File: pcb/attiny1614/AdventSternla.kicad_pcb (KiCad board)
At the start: 2 copper layers, 15 parts, among them J1 5V In, J2 GPIO_C, J3 UPDI, J4 GPIO_A, J5 GPIO_B, J6 NeoPixel Data, J7 Power Out, U1 ATTINY1614

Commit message: Initial layout completed
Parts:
- removed C1: 2200μF 25V, Capacitors_ThroughHole:CP_Radial_D13.0mm_P5.00mm
- removed C2: 1μF 16V, Capacitors_SMD:C_0805_HandSoldering
- removed C3: 100nF 50V, Capacitors_SMD:C_0805_HandSoldering
- removed D1: 5V6 Zener, Diodes_SMD:D_SOT-23_ANK
- removed J1: 5V In, Pin_Headers:Pin_Header_Straight_1x03_Pitch2.54mm
- removed J2: GPIO_C, Pin_Headers:Pin_Header_Straight_1x04_Pitch2.54mm
- removed J3: UPDI, Pin_Headers:Pin_Header_Straight_2x03_Pitch2.54mm
- removed J4: GPIO_A, Pin_Headers:Pin_Header_Straight_1x03_Pitch2.54mm
- removed J5: GPIO_B, Pin_Headers:Pin_Header_Straight_1x04_Pitch2.54mm
- removed J6: NeoPixel Data, Pin_Headers:Pin_Header_Straight_1x02_Pitch2.54mm
- removed J7: Power Out, Pin_Headers:Pin_Header_Straight_1x02_Pitch2.54mm
- removed R1: 250Ω 0.5W, Resistors_SMD:R_1210_HandSoldering
- removed R2: 47kΩ, Resistors_SMD:R_0805_HandSoldering
- removed R3: 4k7Ω, Resistors_SMD:R_0805_HandSoldering
- removed U1: ATTINY1614, SMD_Packages:SOIC-14_N
- added C101: 100nF 50V, Capacitors_SMD:C_0805_HandSoldering, F.Cu at (145.5, 94.5)
- added C102: 1000μF 25V, advent_sternla:CP_Radial_L21.0mm_D13.0mm_P5.00mm_Horizontal, B.Cu at (141.0, 95.5)
- added C103: 1μF 16V, Capacitors_SMD:C_0805_HandSoldering, F.Cu at (149.0, 100.0)
- added D101: 1N4148WSTR, Diodes_SMD:D_SOD-323, F.Cu at (144.5, 100.0)
- added G***: LOGO, advent_sternla:MyBasic_rounded_50_1, F.Cu at (136.8, 103.3)
- added J101: UPDI, advent_sternla:PRG_TC2030-IDC-NL, F.Cu at (163.5, 104.0)
- added J102: NeoPixel Data, Pin_Headers:Pin_Header_Straight_1x02_Pitch2.54mm, F.Cu at (167.9, 93.0)
- added J103: Power Out, Pin_Headers:Pin_Header_Straight_1x02_Pitch2.54mm, F.Cu at (167.9, 98.0)
- added J104: 5V In, advent_sternla:CONN_PWR_JACK_1_3X3_5MM_SOLDER, F.Cu at (143.6, 87.1)
- added J105: GPIO_A, Pin_Headers:Pin_Header_Straight_1x03_Pitch2.54mm, F.Cu at (156.2, 86.2)
- added J106: GPIO_B, Pin_Headers:Pin_Header_Straight_1x04_Pitch2.54mm, F.Cu at (148.0, 104.5)
- added J107: GPIO_C, Pin_Headers:Pin_Header_Straight_1x04_Pitch2.54mm, F.Cu at (167.4, 86.2)
- added R101: 4k7Ω, Resistors_SMD:R_0805_HandSoldering, F.Cu at (163.5, 91.0)
- added R102: 47kΩ, Resistors_SMD:R_0805_HandSoldering, F.Cu at (148.0, 94.5)
- added U101: ATTINY1614, SMD_Packages:SOIC-14_N, F.Cu at (156.0, 95.0)
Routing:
- net /5V: track 0.00 -> 56.1 mm
- net /VDD: track 0.00 -> 42.2 mm
- net /PDI_DATA: track 0.00 -> 27.5 mm, vias 0 -> 2
- net /PA1: track 0.00 -> 16.9 mm, vias 0 -> 1
- net /PB0: track 0.00 -> 15.9 mm
- net /PB2: track 0.00 -> 13.5 mm
- net /PB3: track 0.00 -> 13.3 mm
- net /PA4: track 0.00 -> 9.05 mm
- net /PB1: track 0.00 -> 8.85 mm
- net /PA5: track 0.00 -> 7.93 mm
- net /PA6: track 0.00 -> 7.41 mm
- net /PA3: track 0.00 -> 6.90 mm
- net /PA7: track 0.00 -> 6.88 mm
- net /PA2: track 0.00 -> 6.48 mm
- net /NP_DATA: track 0.00 -> 4.44 mm
- added copper zone on F.Cu, net GND
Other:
- board outline added: 35.6 x 22.4 mm
- net class Default: clearance 0.2 -> 0.1524; trace_width 0.25 -> 0.1524; via_dia 0.6 -> 0.6858; via_drill 0.4 -> 0.3302
- rule pad_to_mask_clearance: 0.2 -> 0
- rule trace_clearance: 0.2 -> 0.1524
- rule trace_min: 0.2 -> 0.1524
- rule via_min_drill: 0.3 -> 0.3302
- rule via_min_size: 0.4 -> 0.6858
- board text added: "+ 5V Out"
- board text added: "5V In"
- board text added: "Data GND Out"
- board text added: "NeoPixel Driver 2L_1"
- board text added: "UDPI"

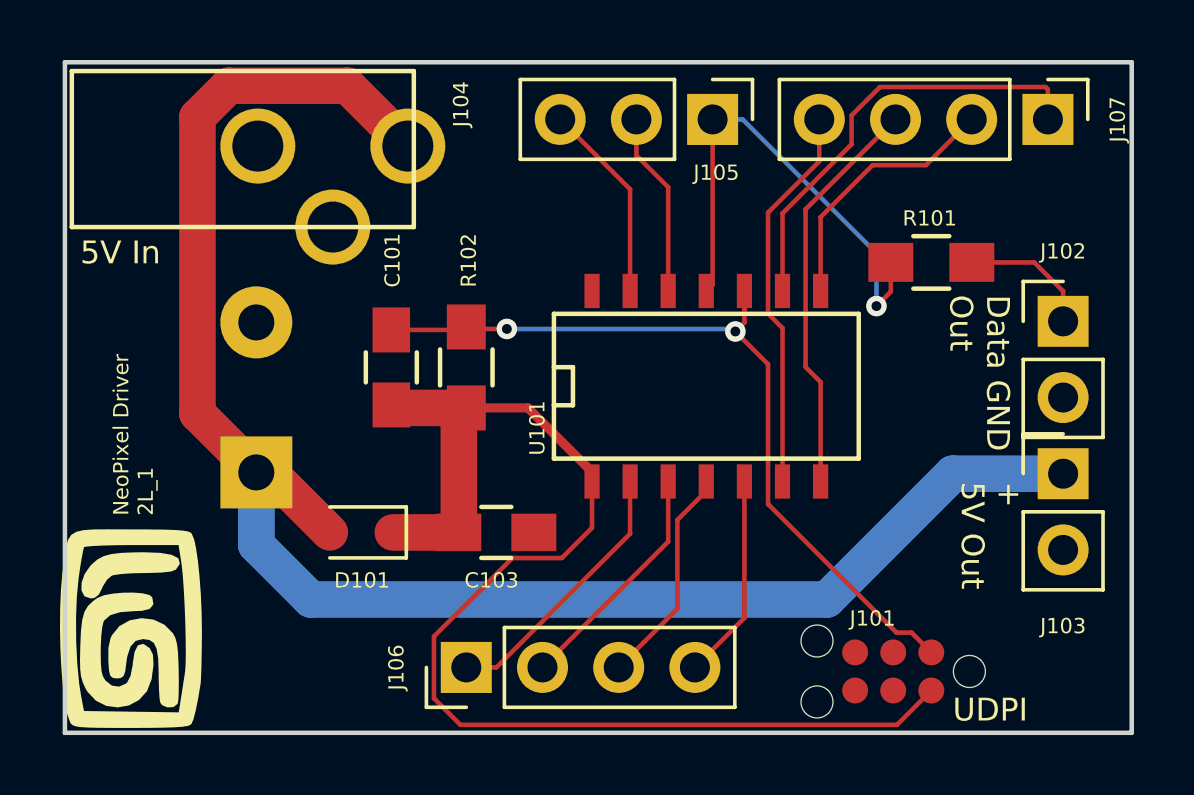
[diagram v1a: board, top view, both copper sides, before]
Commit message: Added some more nomenclature for the pin headers
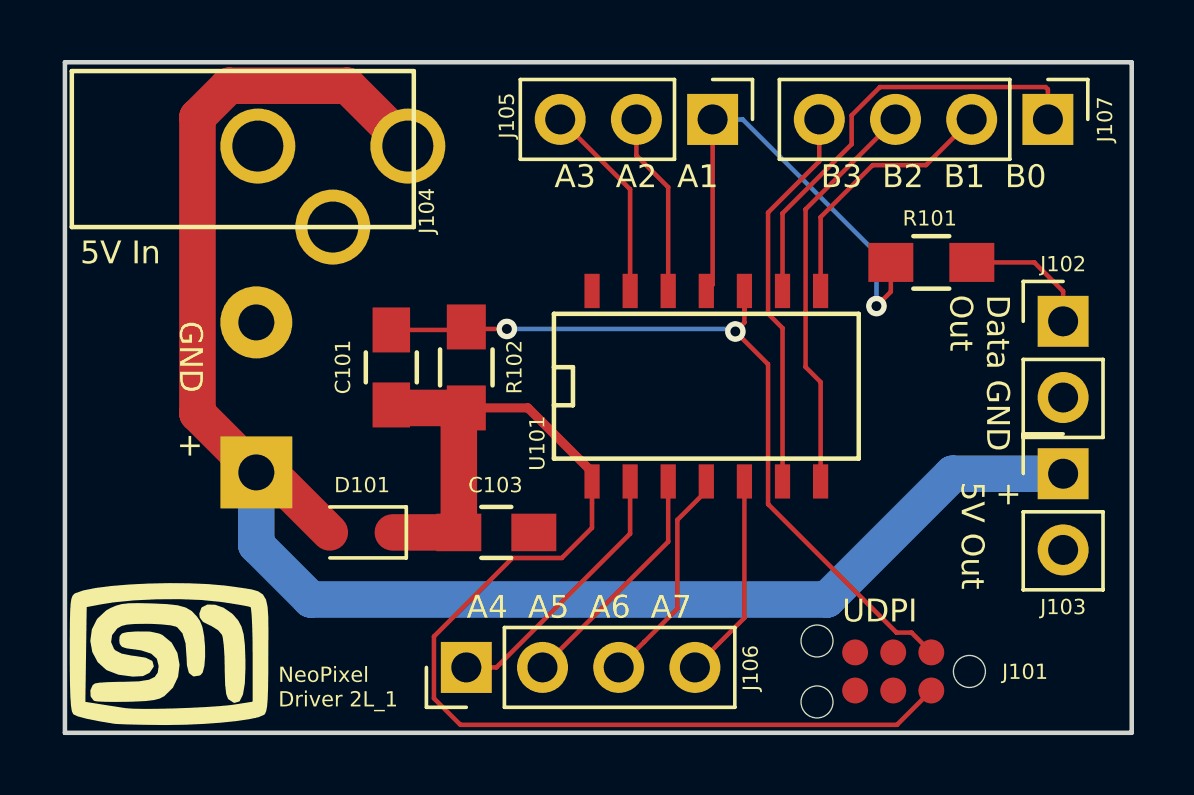
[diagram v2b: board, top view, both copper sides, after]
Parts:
- added G***: LOGO, advent_sternla:MyBasic_rounded_50_1, B.Cu at (138.4, 104.0)
- added G***: LOGO, advent_sternla:KiCad-Logo, B.Cu at (163.8, 104.3)
- moved G*** 1.48 mm to (138.0, 104.0), turned to 0 degrees
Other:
- board text added: "A3 A2 A1"
- board text added: "A4 A5 A6 A7"
- board text added: "B3 B2 B1 B0"
- board text added: "GND +"

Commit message: Added Gerbers and sent to OSH Park
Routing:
- net /5V: track 56.1 -> 49.5 mm
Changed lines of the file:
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@@
 (kicad_pcb (version 4) (host pcbnew 4.0.7)
   (general
-    (links 0)
+    (links 31)
     (no_connects 0)
-    (area 134.544999 84.252999 170.255001 106.755001)
+    (area 134.422599 73.0605 170.743639 107.1623)
     (thickness 1.6)
     (drawings 13)
-    (tracks 101)
+    (tracks 99)
     (zones 0)
     (modules 17)
@@
     (pad_to_mask_clearance 0)
     (aux_axis_origin 0 0)
-    (visible_elements FFFEFF7F)
+    (visible_elements FFFEEF7F)
     (pcbplotparams
-      (layerselection 0x00030_80000001)
+      (layerselection 0x010f0_80000001)
       (usegerberextensions false)
       (excludeedgelayer true)
@@
       (psa4output false)
       (plotreference true)
-      (plotvalue true)
+      (plotvalue false)
       (plotinvisibletext false)
       (padsonsilk false)
@@
       (outputformat 1)
       (mirror false)
-      (drillshape 1)
+      (drillshape 0)
       (scaleselection 1)
-      (outputdirectory ""))
+      (outputdirectory gerber/))
   )
   (net 0 "")
@@
       (rotate (xyz 0 0 0))
     )
-  )
-  (module advent_sternla:CP_Radial_L21.0mm_D13.0mm_P5.00mm_Horizontal (layer B.Cu)
-    (at 141 95.5)
-    (descr "CP, Radial series, Radial, Horizontal, pin pitch=5mm, , length*diameter=21*13mm^2, Electrolytic Capacitor")
-    (tags "CP Radal series Radial Horizontal pin pitch 5mm  length 21mm diameter 13mm Electrolytic Capacitor")
-    (fp_text reference C102 (at 14 0) (layer B.SilkS)
-      (effects (font (size 0.508 0.508) (thickness 0.127)) (justify mirror))
-    )
-    (fp_text value "1000μF 25V" (at 14 -5.06) (layer B.Fab)
-      (effects (font (size 0.508 0.508) (thickness 0.127)) (justify mirror))
-    )
-    (fp_line (start 0 -2.5) (end 3.5 -2.5) (layer B.Fab) (width 0.1))
-    (fp_line (start 1.38 -2.5) (end 3.44 -2.5) (layer B.SilkS) (width 0.12))
-    (fp_line (start 3.5 6.45) (end 3.5 -6.45) (layer B.Fab) (width 0.1))
-    (fp_line (start 24.5 6.45) (end 24.5 -6.45) (layer B.Fab) (width 0.1))
-    (fp_line (start 3.5 6.45) (end 5.24 6.45) (layer B.Fab) (width 0.1))
-    (fp_line (start 5.25 6.44) (end 6.15 5.54) (layer B.Fab) (width 0.1))
-    (fp_line (start 6.15 5.54) (end 7.05 6.44) (layer B.Fab) (width 0.1))
-    (fp_line (start 7.04 6.45) (end 24.5 6.45) (layer B.Fab) (width 0.1))
-    (fp_line (start 3.5 -6.45) (end 5.24 -6.45) (layer B.Fab) (width 0.1))
-    (fp_line (start 5.23 -6.44) (end 6.13 -5.54) (layer B.Fab) (width 0.1))
-    (fp_line (start 6.13 -5.54) (end 7.03 -6.44) (layer B.Fab) (width 0.1))
-    (fp_line (start 7.04 -6.45) (end 24.5 -6.45) (layer B.Fab) (width 0.1))
-    (fp_line (start 0 2.5) (end 3.5 2.5) (layer B.Fab) (width 0.1))
-    (fp_line (start 4.06 2.46) (end 5.86 2.46) (layer B.Fab) (width 0.1))
-    (fp_line (start 4.96 3.36) (end 4.96 1.56) (layer B.Fab) (width 0.1))
-    (fp_line (start 4.06 2.46) (end 5.86 2.46) (layer B.SilkS) (width 0.12))
-    (fp_line (start 4.96 3.36) (end 4.96 1.56) (layer B.SilkS) (width 0.12))
-    (fp_line (start 3.44 6.5) (end 3.44 -6.5) (layer B.SilkS) (width 0.12))
-    (fp_line (start 24.56 6.5) (end 24.56 -6.5) (layer B.SilkS) (width 0.12))
-    (fp_line (start 3.44 6.5) (end 5.24 6.5) (layer B.SilkS) (width 0.12))
-    (fp_line (start 5.25 6.5) (end 6.15 5.6) (layer B.SilkS) (width 0.12))
-    (fp_line (start 6.15 5.6) (end 7.05 6.5) (layer B.SilkS) (width 0.12))
-    (fp_line (start 7.04 6.5) (end 24.56 6.5) (layer B.SilkS) (width 0.12))
-    (fp_line (start 3.44 -6.5) (end 5.24 -6.5) (layer B.SilkS) (width 0.12))
-    (fp_line (start 5.23 -6.5) (end 6.13 -5.6) (layer B.SilkS) (width 0.12))
-    (fp_line (start 6.13 -5.6) (end 7.03 -6.5) (layer B.SilkS) (width 0.12))
-    (fp_line (start 7.04 -6.5) (end 24.56 -6.5) (layer B.SilkS) (width 0.12))
-    (fp_line (start 1.38 2.5) (end 3.44 2.5) (layer B.SilkS) (width 0.12))
-    (fp_line (start -1.45 7) (end -1.45 -7) (layer B.CrtYd) (width 0.05))
-    (fp_line (start -1.45 -7) (end 25 -7) (layer B.CrtYd) (width 0.05))
-    (fp_line (start 25 -7) (end 25 7) (layer B.CrtYd) (width 0.05))
-    (fp_line (start 25 7) (end -1.45 7) (layer B.CrtYd) (width 0.05))
-    (fp_text user %R (at 14 0) (layer B.Fab)
-      (effects (font (size 0.508 0.508) (thickness 0.127)) (justify mirror))
-    )
-    (pad 1 thru_hole rect (at 0 2.5) (size 2.4 2.4) (drill 1.2) (layers *.Cu *.Mask)
-      (net 1 /5V))
-    (pad 2 thru_hole oval (at 0 -2.5) (size 2.4 2.4) (drill 1.2) (layers *.Cu *.Mask)
-      (net 2 GND))
   )
   (module Capacitors_SMD:C_0805_HandSoldering (layer F.Cu)
@@
       (xy -2.775391 -0.969684)) (layer B.SilkS) (width 0.1))
   )
+  (module advent_sternla:CP_Radial_L21.0mm_D13.0mm_P5.00mm_Horizontal (layer B.Cu)
+    (at 141 95.5)
+    (descr "CP, Radial series, Radial, Horizontal, pin pitch=5mm, , length*diameter=21*13mm^2, Electrolytic Capacitor")
+    (tags "CP Radal series Radial Horizontal pin pitch 5mm  length 21mm diameter 13mm Electrolytic Capacitor")
+    (fp_text reference C102 (at 14 0) (layer B.SilkS)
+      (effects (font (size 1 1) (thickness 0.15)) (justify mirror))
+    )
+    (fp_text value "1000μF 25V" (at 14 -5.06) (layer B.Fab)
+      (effects (font (size 1 1) (thickness 0.15)) (justify mirror))
+    )
+    (fp_line (start 0 -2.5) (end 3.5 -2.5) (layer B.Fab) (width 0.1))
+    (fp_line (start 1.38 -2.5) (end 3.44 -2.5) (layer B.SilkS) (width 0.12))
+    (fp_line (start 3.5 6.45) (end 3.5 -6.45) (layer B.Fab) (width 0.1))
+    (fp_line (start 24.5 6.45) (end 24.5 -6.45) (layer B.Fab) (width 0.1))
+    (fp_line (start 3.5 6.45) (end 5.24 6.45) (layer B.Fab) (width 0.1))
+    (fp_line (start 5.25 6.44) (end 6.15 5.54) (layer B.Fab) (width 0.1))
+    (fp_line (start 6.15 5.54) (end 7.05 6.44) (layer B.Fab) (width 0.1))
+    (fp_line (start 7.04 6.45) (end 24.5 6.45) (layer B.Fab) (width 0.1))
+    (fp_line (start 3.5 -6.45) (end 5.24 -6.45) (layer B.Fab) (width 0.1))
+    (fp_line (start 5.23 -6.44) (end 6.13 -5.54) (layer B.Fab) (width 0.1))
+    (fp_line (start 6.13 -5.54) (end 7.03 -6.44) (layer B.Fab) (width 0.1))
+    (fp_line (start 7.04 -6.45) (end 24.5 -6.45) (layer B.Fab) (width 0.1))
+    (fp_line (start 0 2.5) (end 3.5 2.5) (layer B.Fab) (width 0.1))
+    (fp_line (start 4.06 2.46) (end 5.86 2.46) (layer B.Fab) (width 0.1))
+    (fp_line (start 4.96 3.36) (end 4.96 1.56) (layer B.Fab) (width 0.1))
+    (fp_line (start 4.06 2.46) (end 5.86 2.46) (layer B.SilkS) (width 0.12))
+    (fp_line (start 4.96 3.36) (end 4.96 1.56) (layer B.SilkS) (width 0.12))
+    (fp_line (start 3.44 6.5) (end 3.44 -6.5) (layer B.SilkS) (width 0.12))
+    (fp_line (start 24.56 6.5) (end 24.56 -6.5) (layer B.SilkS) (width 0.12))
+    (fp_line (start 3.44 6.5) (end 5.24 6.5) (layer B.SilkS) (width 0.12))
+    (fp_line (start 5.25 6.5) (end 6.15 5.6) (layer B.SilkS) (width 0.12))
+    (fp_line (start 6.15 5.6) (end 7.05 6.5) (layer B.SilkS) (width 0.12))
+    (fp_line (start 7.04 6.5) (end 24.56 6.5) (layer B.SilkS) (width 0.12))
+    (fp_line (start 3.44 -6.5) (end 5.24 -6.5) (layer B.SilkS) (width 0.12))
+    (fp_line (start 5.23 -6.5) (end 6.13 -5.6) (layer B.SilkS) (width 0.12))
+    (fp_line (start 6.13 -5.6) (end 7.03 -6.5) (layer B.SilkS) (width 0.12))
+    (fp_line (start 7.04 -6.5) (end 24.56 -6.5) (layer B.SilkS) (width 0.12))
+    (fp_line (start 1.38 2.5) (end 3.44 2.5) (layer B.SilkS) (width 0.12))
+    (fp_line (start -1.45 7) (end -1.45 -7) (layer B.CrtYd) (width 0.05))
+    (fp_line (start -1.45 -7) (end 25 -7) (layer B.CrtYd) (width 0.05))
+    (fp_line (start 25 -7) (end 25 7) (layer B.CrtYd) (width 0.05))
+    (fp_line (start 25 7) (end -1.45 7) (layer B.CrtYd) (width 0.05))
+    (fp_text user %R (at 14 0) (layer B.Fab)
+      (effects (font (size 1 1) (thickness 0.15)) (justify mirror))
+    )
+    (pad 1 thru_hole rect (at 0 2.5) (size 2.4 2.4) (drill 1.2) (layers *.Cu *.Mask)
+      (net 1 /5V))
+    (pad 2 thru_hole oval (at 0 -2.5) (size 2.4 2.4) (drill 1.2) (layers *.Cu *.Mask)
+      (net 2 GND))
+    (model ../../../../Users/steve/Documents/PCBs/AdventSternla/pcb/modules/3d/CP_Radial_L21.0mm_D13.0mm_P5.00mm_Horizontal.wrl
+      (at (xyz 0 0 0))
+      (scale (xyz 2.54 2.54 2.54))
+      (rotate (xyz -90 0 180))
+    )
+  )
   (gr_text "GND    +" (at 138.811 95.25 270) (layer F.SilkS)
     (effects (font (size 0.762 0.762) (thickness 0.127)))
@@
   (gr_line (start 170.18 84.328) (end 170.18 106.68) (angle 90) (layer Edge.Cuts) (width 0.15))
   (gr_line (start 134.62 84.328) (end 170.18 84.328) (angle 90) (layer Edge.Cuts) (width 0.15))
+  (segment (start 146.05 87.122) (end 146.05 95.3692) (width 1.2192) (layer B.Cu) (net 1))
+  (segment (start 146.05 95.3692) (end 143.4192 98) (width 1.2192) (layer B.Cu) (net 1))
+  (segment (start 143.4192 98) (end 141 98) (width 1.2192) (layer B.Cu) (net 1))
   (segment (start 160.02 102.235) (end 164.211 98.044) (width 1.2192) (layer B.Cu) (net 1))
   (segment (start 164.211 98.044) (end 167.894 98.044) (width 1.2192) (layer B.Cu) (net 1))
@@
   (segment (start 141 98) (end 141 100.4192) (width 1.2192) (layer B.Cu) (net 1))
   (segment (start 141 100.4192) (end 142.8158 102.235) (width 1.2192) (layer B.Cu) (net 1))
-  (segment (start 146.05 87.122) (end 144.037999 85.109999) (width 1.2192) (layer F.Cu) (net 1))
-  (segment (start 144.037999 85.109999) (end 140.084239 85.109999) (width 1.2192) (layer F.Cu) (net 1))
-  (segment (start 140.084239 85.109999) (end 139.037999 86.156239) (width 1.2192) (layer F.Cu) (net 1))
-  (segment (start 139.037999 86.156239) (end 139.037999 96.037999) (width 1.2192) (layer F.Cu) (net 1))
-  (segment (start 139.037999 96.037999) (end 141 98) (width 1.2192) (layer F.Cu) (net 1))
   (segment (start 167.85 98) (end 167.894 98.044) (width 1.2192) (layer B.Cu) (net 1))
   (segment (start 141 98) (end 141.45 98) (width 1.2192) (layer F.Cu) (net 1))

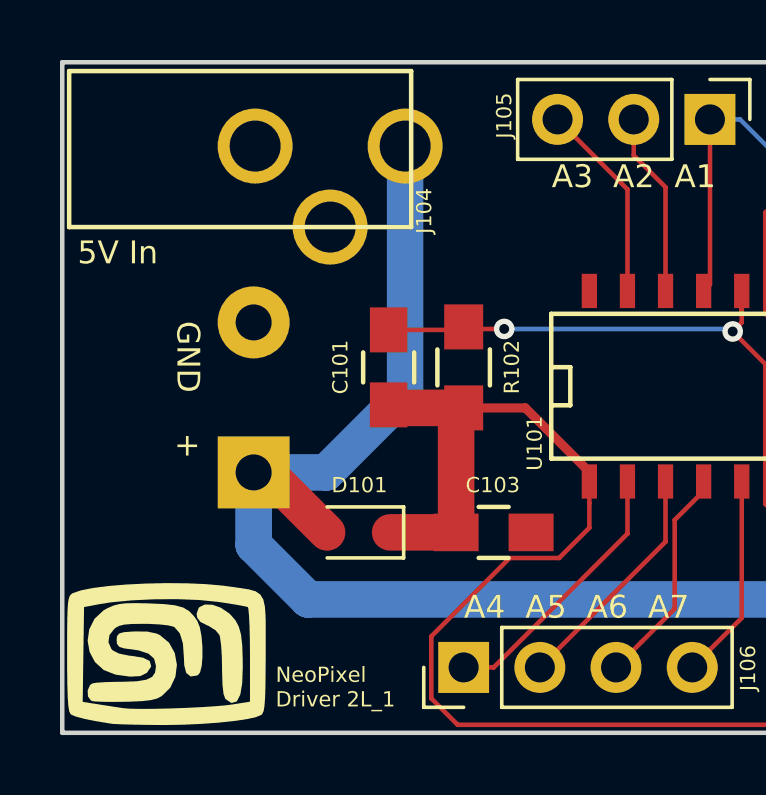
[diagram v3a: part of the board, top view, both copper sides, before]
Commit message: Corrected the diode foot print as with the power jack
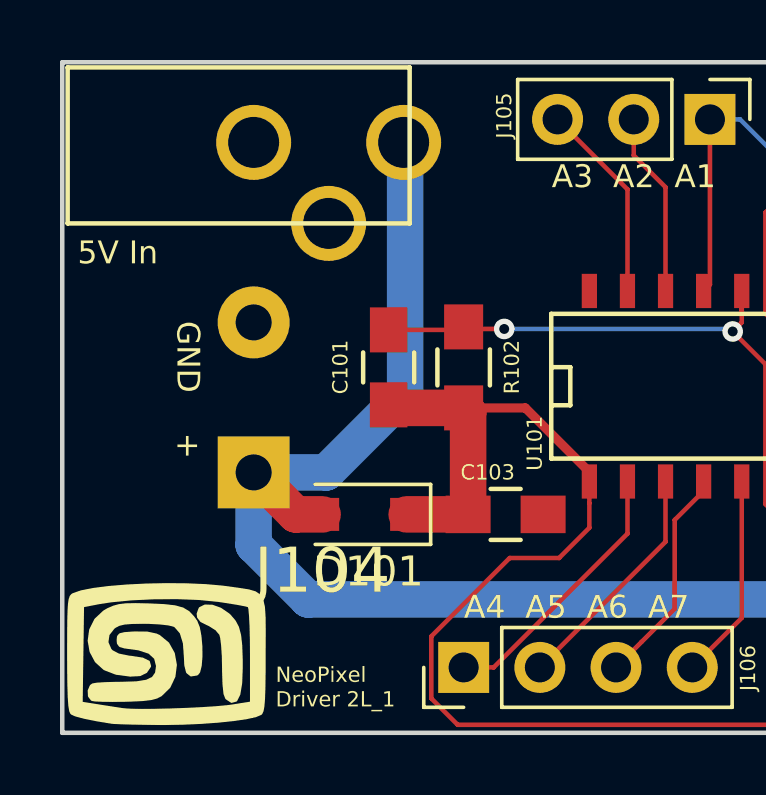
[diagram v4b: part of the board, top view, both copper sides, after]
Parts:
- D101: footprint Diodes_SMD:D_SOD-323 -> Diodes_SMD:D_SOD-123F
- moved C103 0.72 mm to (149.4, 99.4)
- moved D101 0.63 mm to (144.7, 99.4)
- moved J104 0.13 mm to (143.5, 87.0)
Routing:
- net /VDD: track 42.2 -> 41.4 mm
